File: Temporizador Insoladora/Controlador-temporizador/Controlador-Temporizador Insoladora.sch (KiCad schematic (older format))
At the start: 75 parts, among them P1 ICSP, P2 VAC12V, P3 CARGA, P4 TRANSF, P5 VAC, P6 OPTO, P7 CONN_02X08, P8 OPTO, Q1 BC548, Q2 BC548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

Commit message: Casi terminado
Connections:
- net BAJAR: now also U2.36 (RB3/PGM); no longer U2.37 (RB4)
- net GPI1: now also U2.34 (RB1); no longer U2.35 (RB2)
- net INICIAR/PARAR: now also U2.35 (RB2); no longer U2.36 (RB3/PGM)
- net SUBIR: now also U2.37 (RB4); no longer U2.38 (RB5)
- net VCC: no longer P8.1 (P1), U3.1
- new net: P8.1 (P1), U3.1
- no-connect marks 32 -> 31
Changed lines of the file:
@@
 L VCC #PWR06
 U 1 1 552A974E
-P 6200 2800
-F 0 "#PWR06" H 6200 2650 50  0001 C CNN
-F 1 "VCC" H 6200 2950 50  0000 C CNN
-F 2 "" H 6200 2800 60  0000 C CNN
-F 3 "" H 6200 2800 60  0000 C CNN
-	1    6200 2800
+P 6400 2850
+F 0 "#PWR06" H 6400 2700 50  0001 C CNN
+F 1 "VCC" H 6400 3000 50  0000 C CNN
+F 2 "" H 6400 2850 60  0000 C CNN
+F 3 "" H 6400 2850 60  0000 C CNN
+	1    6400 2850
 	1    0    0    -1
 $EndComp
@@
 	6100 2150 5650 2150
 Wire Wire Line
-	6200 2800 6200 2850
-Wire Wire Line
-	6200 2850 5650 2850
+	5650 2850 6400 2850
 Wire Wire Line
 	6200 3000 6200 2950
@@
 Connection ~ 5500 6250
 Wire Wire Line
-	5800 2750 5650 2750
+	6050 2750 5650 2750
 Wire Wire Line
 	5800 6250 5500 6250
@@
 Wire Wire Line
 	10250 2900 10250 3150
-$Comp
-L VCC #PWR021
-U 1 1 552AC1EA
-P 10250 2750
-F 0 "#PWR021" H 10250 2600 50  0001 C CNN
-F 1 "VCC" H 10250 2900 50  0000 C CNN
-F 2 "" H 10250 2750 60  0000 C CNN
-F 3 "" H 10250 2750 60  0000 C CNN
-	1    10250 2750
-	1    0    0    -1
-$EndComp
 Wire Wire Line
 	10250 2750 10250 2800
@@
 Connection ~ 12250 3400
 $Comp
-L VCC #PWR022
+L VCC #PWR021
 U 1 1 552AD000
 P 2150 3650
-F 0 "#PWR022" H 2150 3500 50  0001 C CNN
+F 0 "#PWR021" H 2150 3500 50  0001 C CNN
 F 1 "VCC" H 2150 3800 50  0000 C CNN
 F 2 "" H 2150 3650 60  0000 C CNN
@@
 $EndComp
 $Comp
-L GND #PWR023
+L GND #PWR022
 U 1 1 552AD006
 P 2150 4150
-F 0 "#PWR023" H 2150 3900 50  0001 C CNN
+F 0 "#PWR022" H 2150 3900 50  0001 C CNN
 F 1 "GND" H 2150 4000 50  0000 C CNN
 F 2 "" H 2150 4150 60  0000 C CNN
@@
 	2150 3650 2150 3750
 $Comp
-L VCC #PWR024
+L VCC #PWR023
 U 1 1 552AD090
 P 1100 4600
-F 0 "#PWR024" H 1100 4450 50  0001 C CNN
+F 0 "#PWR023" H 1100 4450 50  0001 C CNN
 F 1 "VCC" H 1100 4750 50  0000 C CNN
 F 2 "" H 1100 4600 60  0000 C CNN
@@
 $EndComp
 $Comp
-L GND #PWR025
+L GND #PWR024
 U 1 1 552AD096
 P 1100 5100
-F 0 "#PWR025" H 1100 4850 50  0001 C CNN
+F 0 "#PWR024" H 1100 4850 50  0001 C CNN
 F 1 "GND" H 1100 4950 50  0000 C CNN
 F 2 "" H 1100 5100 60  0000 C CNN
@@
 	14050 2950 14200 2950
 $Comp
-L Earth #PWR026
+L Earth #PWR025
 U 1 1 552AE860
 P 14050 3100
-F 0 "#PWR026" H 14050 2850 50  0001 C CNN
+F 0 "#PWR025" H 14050 2850 50  0001 C CNN
 F 1 "Earth" H 14050 2950 50  0001 C CNN
 F 2 "" H 14050 3100 60  0000 C CNN
@@
 $EndComp
 $Comp
-L GND #PWR027
+L GND #PWR026
 U 1 1 552B01E5
 P 7900 6750
-F 0 "#PWR027" H 7900 6500 50  0001 C CNN
+F 0 "#PWR026" H 7900 6500 50  0001 C CNN
 F 1 "GND" H 7900 6600 50  0000 C CNN
 F 2 "" H 7900 6750 60  0000 C CNN
@@
 $EndComp
 $Comp
-L VCC #PWR028
+L VCC #PWR027
 U 1 1 552B0938
 P 7900 5150
-F 0 "#PWR028" H 7900 5000 50  0001 C CNN
+F 0 "#PWR027" H 7900 5000 50  0001 C CNN
 F 1 "VCC" H 7900 5300 50  0000 C CNN
 F 2 "" H 7900 5150 60  0000 C CNN
@@
 Text GLabel 7050 5800 2    60   Input ~ 0
 SUBIR
-Text GLabel 6350 2250 2    60   Input ~ 0
+Text GLabel 6100 2350 2    60   Input ~ 0
 SUBIR
 Wire Wire Line
-	6350 2250 5650 2250
-Wire Wire Line
-	5750 2350 5650 2350
-Wire Wire Line
-	5650 2450 6100 2450
+	5650 2350 6100 2350
 $Comp
 L Crystal_Small Y1
@@
 	2900 2950 2900 2750
 $Comp
-L GND #PWR029
+L GND #PWR028
 U 1 1 552B5011
 P 3150 2500
-F 0 "#PWR029" H 3150 2250 50  0001 C CNN
+F 0 "#PWR028" H 3150 2250 50  0001 C CNN
 F 1 "GND" H 3150 2350 50  0000 C CNN
 F 2 "" H 3150 2500 60  0000 C CNN
@@
 Connection ~ 9100 5800
 Wire Wire Line
-	5750 2550 5650 2550
-Wire Wire Line
 	12800 2400 12800 2150
 Wire Wire Line
@@
 $EndComp
 $Comp
-L GND #PWR030
+L GND #PWR029
 U 1 1 552AC31E
 P 4000 10450
-F 0 "#PWR030" H 4000 10200 50  0001 C CNN
+F 0 "#PWR029" H 4000 10200 50  0001 C CNN
 F 1 "GND" H 4000 10300 50  0000 C CNN
 F 2 "" H 4000 10450 60  0000 C CNN
@@
 	2000 6000 2000 5750
 $Comp
-L PWR_FLAG #FLG031
+L PWR_FLAG #FLG030
 U 1 1 552BA99D
 P 10050 4700
-F 0 "#FLG031" H 10050 4795 50  0001 C CNN
+F 0 "#FLG030" H 10050 4795 50  0001 C CNN
 F 1 "PWR_FLAG" H 10050 4880 50  0000 C CNN
 F 2 "" H 10050 4700 60  0000 C CNN
@@
 $EndComp
 $Comp
-L GND #PWR032
+L GND #PWR031
 U 1 1 552BAA37
 P 10050 4700
-F 0 "#PWR032" H 10050 4450 50  0001 C CNN
+F 0 "#PWR031" H 10050 4450 50  0001 C CNN
 F 1 "GND" H 10050 4550 50  0000 C CNN
 F 2 "" H 10050 4700 60  0000 C CNN
@@
 $EndComp
 $Comp
-L GND #PWR033
+L GND #PWR032
 U 1 1 552BD498
 P 6450 10450
-F 0 "#PWR033" H 6450 10200 50  0001 C CNN
+F 0 "#PWR032" H 6450 10200 50  0001 C CNN
 F 1 "GND" H 6450 10300 50  0000 C CNN
 F 2 "" H 6450 10450 60  0000 C CNN
@@
 $EndComp
 $Comp
-L GND #PWR034
+L GND #PWR033
 U 1 1 552BDAE3
 P 8900 10450
-F 0 "#PWR034" H 8900 10200 50  0001 C CNN
+F 0 "#PWR033" H 8900 10200 50  0001 C CNN
 F 1 "GND" H 8900 10300 50  0000 C CNN
 F 2 "" H 8900 10450 60  0000 C CNN
@@
 NoConn ~ 3950 2850
 NoConn ~ 3950 2950
-NoConn ~ 5650 2650
-$Comp
-L PWR_FLAG #FLG035
+$Comp
+L PWR_FLAG #FLG034
 U 1 1 552B274E
 P 10500 4700
-F 0 "#FLG035" H 10500 4795 50  0001 C CNN
+F 0 "#FLG034" H 10500 4795 50  0001 C CNN
 F 1 "PWR_FLAG" H 10500 4880 50  0000 C CNN
 F 2 "" H 10500 4700 60  0000 C CNN
@@
 $EndComp
 $Comp
-L Earth #PWR036
+L Earth #PWR035
 U 1 1 552B349E
 P 10500 4700
-F 0 "#PWR036" H 10500 4450 50  0001 C CNN
+F 0 "#PWR035" H 10500 4450 50  0001 C CNN
 F 1 "Earth" H 10500 4550 50  0001 C CNN
 F 2 "" H 10500 4700 60  0000 C CNN
@@
 NoConn ~ 3950 2850
 NoConn ~ 3950 2950
-NoConn ~ 5650 2650
 Wire Wire Line
 	6900 5350 10050 5350
@@
 $EndComp
 $Comp
-L GND #PWR037
+L GND #PWR036
 U 1 1 552BDC57
 P 10550 10450
-F 0 "#PWR037" H 10550 10200 50  0001 C CNN
+F 0 "#PWR036" H 10550 10200 50  0001 C CNN
 F 1 "GND" H 10550 10300 50  0000 C CNN
 F 2 "" H 10550 10450 60  0000 C CNN
@@
 Text GLabel 7900 10050 0    60   Input ~ 0
 SEGD
-Text GLabel 6100 2450 2    60   Input ~ 0
+Text GLabel 6100 2550 2    60   Input ~ 0
 INICIAR/PARAR
-Text GLabel 5750 2350 2    60   Input ~ 0
+Text GLabel 5750 2450 2    60   Input ~ 0
 BAJAR
 Text GLabel 5750 4600 0    60   Input ~ 0
@@
 Text Label 2450 9400 2    60   ~ 0
 RD7
-Text GLabel 5750 2550 2    60   Input ~ 0
+Text GLabel 5750 2650 2    60   Input ~ 0
 GPI1
-Text GLabel 5800 2750 2    60   Input ~ 0
+Text GLabel 6050 2750 2    60   Input ~ 0
 CPZ
 Text GLabel 10250 5800 2    60   Input ~ 0
@@
 Connection ~ 10250 3000
 $Comp
-L VCC #PWR038
+L VCC #PWR037
 U 1 1 554272CB
 P 8050 3400
-F 0 "#PWR038" H 8050 3250 50  0001 C CNN
+F 0 "#PWR037" H 8050 3250 50  0001 C CNN
 F 1 "VCC" H 8050 3550 50  0000 C CNN
 F 2 "" H 8050 3400 60  0000 C CNN
@@
 	8050 3700 8100 3700
 Wire Wire Line
-	8100 3900 7050 3900
+	7050 3900 8100 3900
 Wire Wire Line
 	7050 3900 7050 4400
@@
 Connection ~ 8050 3550
 Connection ~ 7900 3900
+Wire Wire Line
+	5750 2650 5650 2650
+Wire Wire Line
+	5650 2550 6100 2550
+Wire Wire Line
+	5650 2450 5750 2450
+NoConn ~ 5650 2250
 $EndSCHEMATC

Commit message: casi terminado el ruteado de la placa controlador
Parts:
- removed P8: OPTO, Connect:bornier3, symbol CONN_01X03
- added P8: OPTO, Connect:bornier2, symbol CONN_01X02
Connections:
- net at R15.2: now also P8.2 (P2)
- net at U3.1: now also P8.1 (P1)
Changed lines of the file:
@@
 	10500 3000 10250 3000
-Wire Wire Line
-	10250 2900 10250 3150
 Wire Wire Line
 	10250 2750 10250 2800
@@
 Wire Wire Line
 	3350 3750 3950 3750
-$Comp
-L CONN_01X03 P8
-U 1 1 554268AC
-P 9700 2900
-F 0 "P8" H 9700 3100 50  0000 C CNN
-F 1 "OPTO" V 9800 2900 50  0000 C CNN
-F 2 "Connect:bornier3" H 9700 2900 60  0001 C CNN
-F 3 "" H 9700 2900 60  0000 C CNN
-	1    9700 2900
-	-1   0    0    -1
-$EndComp
 Connection ~ 10250 2800
 Wire Wire Line
-	9900 3000 9900 3650
+	9900 2900 9900 3650
 Wire Wire Line
 	9900 3650 10250 3650
-Wire Wire Line
-	9900 2900 10250 2900
 Connection ~ 10250 3000
 $Comp
@@
 	5650 2450 5750 2450
 NoConn ~ 5650 2250
+Wire Wire Line
+	10250 3000 10250 3150
+$Comp
+L CONN_01X02 P8
+U 1 1 55443048
+P 9700 2850
+F 0 "P8" H 9700 3000 50  0000 C CNN
+F 1 "OPTO" V 9800 2850 50  0000 C CNN
+F 2 "Connect:bornier2" H 9700 2850 60  0001 C CNN
+F 3 "" H 9700 2850 60  0000 C CNN
+	1    9700 2850
+	-1   0    0    -1
+$EndComp
 $EndSCHEMATC

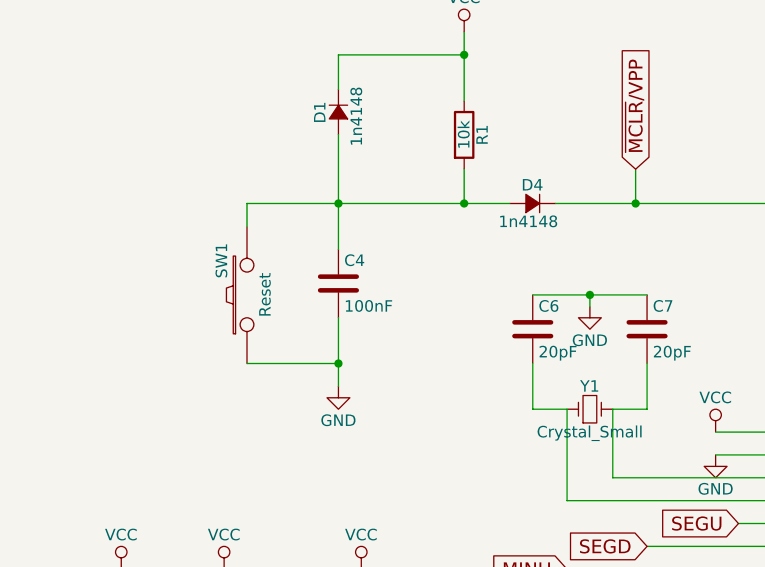
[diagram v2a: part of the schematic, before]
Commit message: Quitado pulsador de reset por ser irrelevante para la aplicación
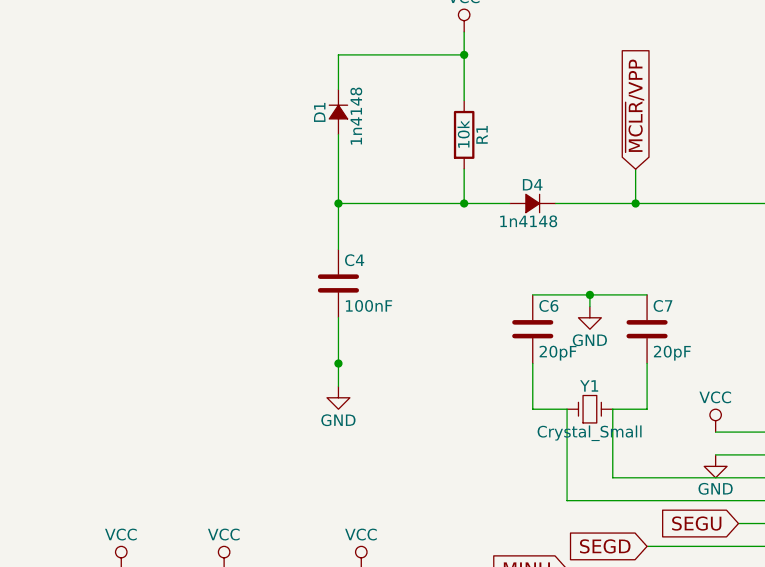
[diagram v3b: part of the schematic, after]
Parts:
- removed SW1: Reset, Buttons_Switches_ThroughHole:SW_PUSH_SMALL, symbol SW_PUSH
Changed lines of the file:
@@
-$EndComp
-$Comp
-L SW_PUSH SW1
-U 1 1 552A8EB5
-P 1650 2450
-F 0 "SW1" H 1800 2560 50  0000 C CNN
-F 1 "Reset" H 1650 2370 50  0000 C CNN
-F 2 "Buttons_Switches_ThroughHole:SW_PUSH_SMALL" H 1650 2450 60  0001 C CNN
-F 3 "" H 1650 2450 60  0000 C CNN
-	1    1650 2450
-	0    -1   -1   0
 $EndComp
 $Comp
@@
 	2050 1750 2050 2250
 Wire Wire Line
-	1650 2050 2800 2050
-Wire Wire Line
 	2600 2050 2600 1900
 Connection ~ 2050 2050
 Wire Wire Line
 	2050 2550 2050 2850
-Wire Wire Line
-	1650 2150 1650 2050
-Wire Wire Line
-	1650 2750 2050 2750
 Connection ~ 2050 2750
 Connection ~ 2600 2050
@@
 	-1   0    0    -1
 $EndComp
+Wire Wire Line
+	2050 2050 2800 2050
 $EndSCHEMATC

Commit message: Reacomodando controlador
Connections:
- net Xtal+: now reaches C7.2, U2.13 (OSC1/CLKI), Y1.2
- net Xtal-: now reaches C6.2, U2.14 (OSC2/CLKO), Y1.1
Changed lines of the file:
@@
 Wire Wire Line
 	2050 2050 2800 2050
+Text Label 3350 3250 0    60   ~ 0
+Xtal+
+Text Label 3200 3350 0    60   ~ 0
+Xtal-
 $EndSCHEMATC

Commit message: Acomodando controlador
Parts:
- removed D6: 1N4007, Diodes_ThroughHole:Diode_DO-41_SOD81_Horizontal_RM10, symbol D_Small
- added P9: OPTO, Connect:bornier2, symbol CONN_01X02
- added Q7: BC548, Housings_TO-92:TO-92_Inline_Wide, symbol BC548
- added R30: 1K, Discret:R3, symbol R
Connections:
- net GND: now also Q7.3 (E)
- net VCC: now also P9.1 (P1)
- net SALIDAOPTO1: now reaches U2.24 (RC5)
- net SALIDAOPTO1: now also R30.2
- net SALIDAOPTO renamed SALIDAOPTO0
- new net: Q7.2 (B), R30.1
- new net: P9.2 (P2), Q7.1 (C)
- no-connect marks 31 -> 29
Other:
- moved on the sheet: P6, Q1, R13
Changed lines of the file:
@@
 L R R13
 U 1 1 552AB8A1
-P 6300 4600
-F 0 "R13" V 6380 4600 50  0000 C CNN
-F 1 "1K" V 6300 4600 50  0000 C CNN
-F 2 "Discret:R3" V 6230 4600 30  0001 C CNN
-F 3 "" H 6300 4600 30  0000 C CNN
-	1    6300 4600
+P 7950 1750
+F 0 "R13" V 8030 1750 50  0000 C CNN
+F 1 "1K" V 7950 1750 50  0000 C CNN
+F 2 "Discret:R3" V 7880 1750 30  0001 C CNN
+F 3 "" H 7950 1750 30  0000 C CNN
+	1    7950 1750
 	0    1    1    0
 $EndComp
@@
 	5800 6250 5500 6250
 Wire Wire Line
-	6750 4600 6450 4600
-Wire Wire Line
-	6150 4600 5750 4600
+	8200 1750 8100 1750
+Wire Wire Line
+	7800 1750 7700 1750
 $Comp
 L GND #PWR020
 U 1 1 552ABE02
-P 7050 4950
-F 0 "#PWR020" H 7050 4700 50  0001 C CNN
-F 1 "GND" H 7050 4800 50  0000 C CNN
-F 2 "" H 7050 4950 60  0000 C CNN
-F 3 "" H 7050 4950 60  0000 C CNN
-	1    7050 4950
-	1    0    0    -1
-$EndComp
-Wire Wire Line
-	7050 4950 7050 4800
+P 8500 2050
+F 0 "#PWR020" H 8500 1800 50  0001 C CNN
+F 1 "GND" H 8500 1900 50  0000 C CNN
+F 2 "" H 8500 2050 60  0000 C CNN
+F 3 "" H 8500 2050 60  0000 C CNN
+	1    8500 2050
+	1    0    0    -1
+$EndComp
+Wire Wire Line
+	8500 2050 8500 1950
 $Comp
 L R R15
@@
 L BC548 Q1
 U 1 1 552AC2A5
-P 6950 4600
-F 0 "Q1" H 7150 4675 50  0000 L CNN
-F 1 "BC548" H 7150 4600 50  0000 L CNN
-F 2 "Housings_TO-92:TO-92_Inline_Wide" H 7150 4525 50  0000 L CIN
-F 3 "" H 6950 4600 50  0000 L CNN
-	1    6950 4600
+P 8400 1750
+F 0 "Q1" H 8600 1825 50  0000 L CNN
+F 1 "BC548" H 8600 1750 50  0000 L CNN
+F 2 "Housings_TO-92:TO-92_Inline_Wide" H 8600 1675 50  0000 L CIN
+F 3 "" H 8400 1750 50  0000 L CNN
+	1    8400 1750
 	1    0    0    -1
 $EndComp
@@
 NoConn ~ 5650 3450
 NoConn ~ 5650 3550
-NoConn ~ 5650 3650
 NoConn ~ 3950 2150
 NoConn ~ 3950 2250
@@
 NoConn ~ 5650 3450
 NoConn ~ 5650 3550
-NoConn ~ 5650 3650
 NoConn ~ 3950 2150
 NoConn ~ 3950 2250
@@
 Text GLabel 5750 2450 2    60   Input ~ 0
 BAJAR
-Text GLabel 5750 4600 0    60   Input ~ 0
-SALIDAOPTO
+Text GLabel 7700 1750 0    60   Input ~ 0
+SALIDAOPTO0
 Text GLabel 6250 3750 2    60   Input ~ 0
-SALIDAOPTO
+SALIDAOPTO0
 Text GLabel 3350 1900 1    60   Input ~ 0
 ~MCLR~/VPP
@@
 L VCC #PWR037
 U 1 1 554272CB
-P 8050 3400
-F 0 "#PWR037" H 8050 3250 50  0001 C CNN
-F 1 "VCC" H 8050 3550 50  0000 C CNN
-F 2 "" H 8050 3400 60  0000 C CNN
-F 3 "" H 8050 3400 60  0000 C CNN
-	1    8050 3400
-	1    0    0    -1
-$EndComp
-Wire Wire Line
-	8050 3400 8050 3700
-Wire Wire Line
-	8050 3700 8100 3700
-Wire Wire Line
-	7050 3900 8100 3900
-Wire Wire Line
-	7050 3900 7050 4400
+P 8550 900
+F 0 "#PWR037" H 8550 750 50  0001 C CNN
+F 1 "VCC" H 8550 1050 50  0000 C CNN
+F 2 "" H 8550 900 60  0000 C CNN
+F 3 "" H 8550 900 60  0000 C CNN
+	1    8550 900
+	1    0    0    -1
+$EndComp
+Wire Wire Line
+	8550 900  8550 1200
 $Comp
 L CONN_01X02 P6
 U 1 1 55427985
-P 8300 3750
-F 0 "P6" H 8300 3900 50  0000 C CNN
-F 1 "OPTO" V 8400 3750 50  0000 C CNN
-F 2 "Connect:bornier2" H 8300 3750 60  0001 C CNN
-F 3 "" H 8300 3750 60  0000 C CNN
-	1    8300 3750
-	1    0    0    -1
-$EndComp
-Wire Wire Line
-	8100 3900 8100 3800
-$Comp
-L D_Small D6
-U 1 1 554285F2
-P 7900 3800
-F 0 "D6" H 7850 3880 50  0000 L CNN
-F 1 "1N4007" H 7800 4000 50  0000 L CNN
-F 2 "Diodes_ThroughHole:Diode_DO-41_SOD81_Horizontal_RM10" V 7900 3800 60  0001 C CNN
-F 3 "" V 7900 3800 60  0000 C CNN
-	1    7900 3800
-	0    -1   -1   0
-$EndComp
-Wire Wire Line
-	7900 3700 7900 3550
-Wire Wire Line
-	7900 3550 8050 3550
-Connection ~ 8050 3550
-Connection ~ 7900 3900
+P 8750 1250
+F 0 "P6" H 8750 1400 50  0000 C CNN
+F 1 "OPTO" V 8850 1250 50  0000 C CNN
+F 2 "Connect:bornier2" H 8750 1250 60  0001 C CNN
+F 3 "" H 8750 1250 60  0000 C CNN
+	1    8750 1250
+	1    0    0    -1
+$EndComp
+Wire Wire Line
+	8550 1400 8550 1300
+Wire Wire Line
+	8350 1200 8350 1050
+Wire Wire Line
+	8350 1050 8550 1050
+Connection ~ 8550 1050
+Connection ~ 8350 1400
 Wire Wire Line
 	5750 2650 5650 2650
@@
 Text Label 3200 3350 0    60   ~ 0
 Xtal-
+Wire Wire Line
+	8350 1400 8550 1400
+Connection ~ 8500 1400
+Wire Wire Line
+	8500 1550 8500 1400
+$Comp
+L R R30
+U 1 1 555AA8C0
+P 7900 3300
+F 0 "R30" V 7980 3300 50  0000 C CNN
+F 1 "1K" V 7900 3300 50  0000 C CNN
+F 2 "Discret:R3" V 7830 3300 30  0001 C CNN
+F 3 "" H 7900 3300 30  0000 C CNN
+	1    7900 3300
+	0    1    1    0
+$EndComp
+Wire Wire Line
+	8150 3300 8050 3300
+Wire Wire Line
+	7750 3300 7650 3300
+$Comp
+L GND #PWR038
+U 1 1 555AA8C8
+P 8450 3600
+F 0 "#PWR038" H 8450 3350 50  0001 C CNN
+F 1 "GND" H 8450 3450 50  0000 C CNN
+F 2 "" H 8450 3600 60  0000 C CNN
+F 3 "" H 8450 3600 60  0000 C CNN
+	1    8450 3600
+	1    0    0    -1
+$EndComp
+Wire Wire Line
+	8450 3600 8450 3500
+$Comp
+L BC548 Q7
+U 1 1 555AA8CF
+P 8350 3300
+F 0 "Q7" H 8550 3375 50  0000 L CNN
+F 1 "BC548" H 8550 3300 50  0000 L CNN
+F 2 "Housings_TO-92:TO-92_Inline_Wide" H 8550 3225 50  0000 L CIN
+F 3 "" H 8350 3300 50  0000 L CNN
+	1    8350 3300
+	1    0    0    -1
+$EndComp
+Text GLabel 7650 3300 0    60   Input ~ 0
+SALIDAOPTO1
+$Comp
+L VCC #PWR039
+U 1 1 555AA8D6
+P 8500 2450
+F 0 "#PWR039" H 8500 2300 50  0001 C CNN
+F 1 "VCC" H 8500 2600 50  0000 C CNN
+F 2 "" H 8500 2450 60  0000 C CNN
+F 3 "" H 8500 2450 60  0000 C CNN
+	1    8500 2450
+	1    0    0    -1
+$EndComp
+Wire Wire Line
+	8500 2450 8500 2750
+$Comp
+L CONN_01X02 P9
+U 1 1 555AA8DF
+P 8700 2800
+F 0 "P9" H 8700 2950 50  0000 C CNN
+F 1 "OPTO" V 8800 2800 50  0000 C CNN
+F 2 "Connect:bornier2" H 8700 2800 60  0001 C CNN
+F 3 "" H 8700 2800 60  0000 C CNN
+	1    8700 2800
+	1    0    0    -1
+$EndComp
+Wire Wire Line
+	8500 2950 8500 2850
+Wire Wire Line
+	8300 2750 8300 2600
+Wire Wire Line
+	8300 2600 8500 2600
+Connection ~ 8500 2600
+Connection ~ 8300 2950
+Wire Wire Line
+	8300 2950 8500 2950
+Connection ~ 8450 2950
+Wire Wire Line
+	8450 3100 8450 2950
+Text GLabel 6250 3650 2    60   Input ~ 0
+SALIDAOPTO1
+Wire Wire Line
+	6250 3650 5650 3650
 $EndSCHEMATC
